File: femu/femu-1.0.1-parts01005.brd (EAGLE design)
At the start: 24.1 x 15.8 mm, 54 parts, among them IC1 ESP32-QFN_5X5, IC3 FT230XQ

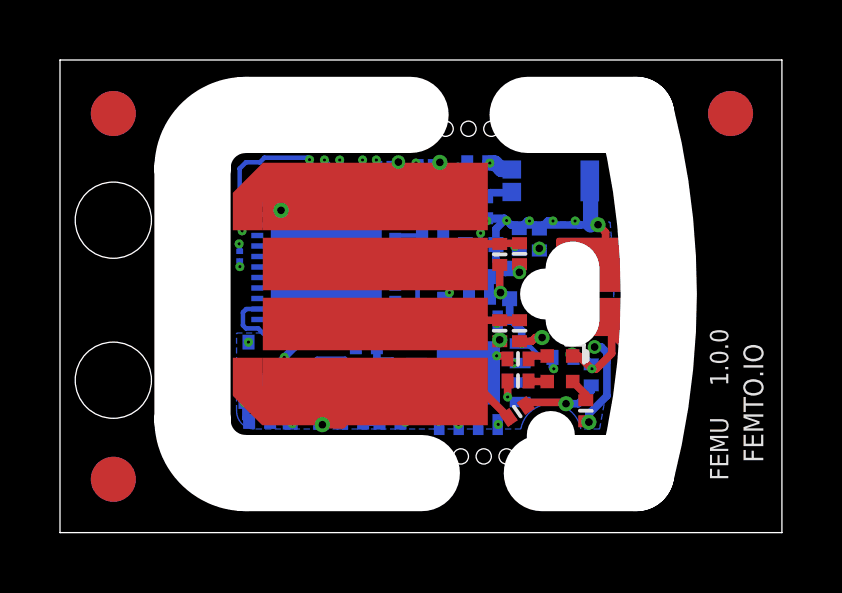
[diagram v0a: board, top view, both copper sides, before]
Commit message: Updating BoM to use the FT231XQ
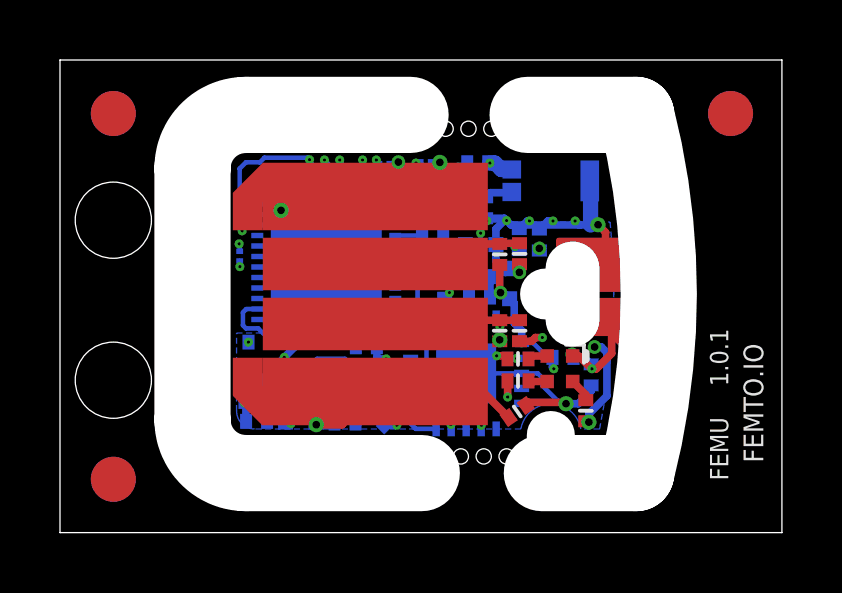
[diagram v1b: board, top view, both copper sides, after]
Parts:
- removed IC3: FT230XQ, ftdichip:QFN16
- added U$11: FT231XQ, ftdi_ft231x:QFN-20_4X4
- moved C27 0.43 mm to (10.6, 3.84), turned to 225 degrees
- moved C23 0.26 mm to (9.50, 3.66)
- moved C5 0.18 mm to (10.2, 4.75)
- moved FB1 0.15 mm to (8.03, 3.68)
- moved C4 0.10 mm to (10.2, 5.44)
- moved C2 0.10 mm to (6.55, 3.71)
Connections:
- removed net BOOT/CTS: IC1.23, IC3.4
- new net BOOT/DTR: IC1.23, U$11.18
- net 3.3V: now also U$11.10, U$11.11, U$11.20; no longer IC3.1, IC3.8, IC3.9
- net EN/RTS: now also U$11.19; no longer IC3.16
- net GND: now also U$11.13, U$11.21, U$11.3; no longer IC3.13, IC3.3
- net RXD: now also U$11.1; no longer IC3.15
- net TXD: now also U$11.17; no longer IC3.2
- net USB+: now also U$11.8; no longer IC3.6
- net USB-: now also U$11.9; no longer IC3.7
- net VIN: now also U$11.12; no longer IC3.10
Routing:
- net BOOT/DTR: track 0.00 -> 10.5 mm, vias 0 -> 2
- net RXD: track 21.7 -> 13.3 mm
- net TXD: track 11.7 -> 17.7 mm
- net BOOT/CTS: track 5.56 -> 0.00 mm, vias 2 -> 0
- net 3.3V: track 63.0 -> 64.0 mm
- net XIN: track 14.3 -> 13.5 mm
- net GND: track 73.4 -> 74.1 mm
- net VIN: track 11.0 -> 11.5 mm
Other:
- board text added: "1.0.1"
- board text removed: "1.0.0"
